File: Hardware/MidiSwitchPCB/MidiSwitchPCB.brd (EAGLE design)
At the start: 180 x 100 mm, 78 parts, among them IC3 74LVC2G04GW,125, J1 694108106102, J2 NMJ6HCD2, J3 NMJ6HCD2, J4 NMJ6HCD2, J5 NMJ6HCD2, Q1 BSS123, Q2 BSS123, Q3 BSS123, Q4 BSS123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

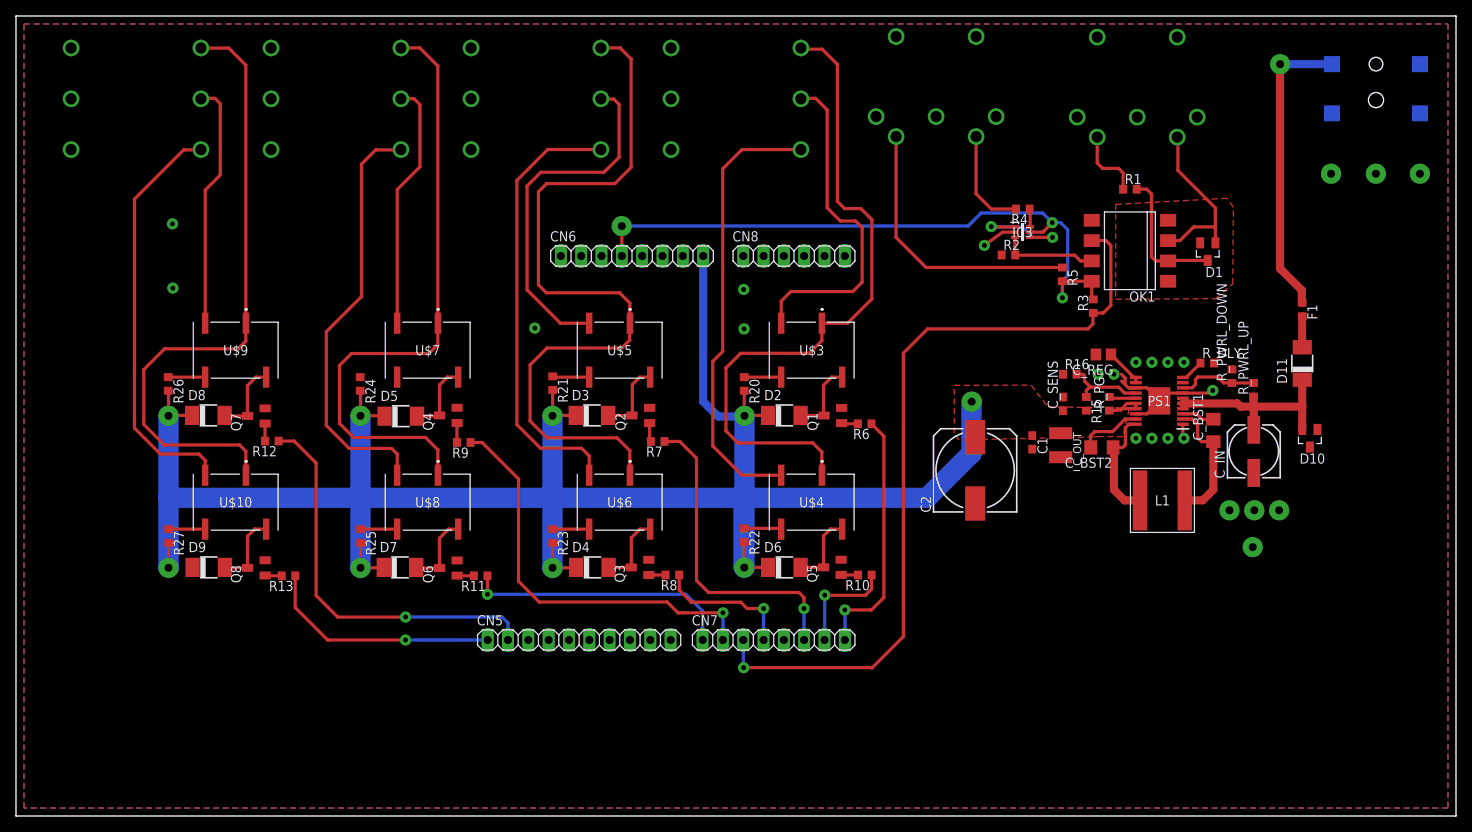
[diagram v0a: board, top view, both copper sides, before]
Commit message: Changed PCB size to 160 x 100
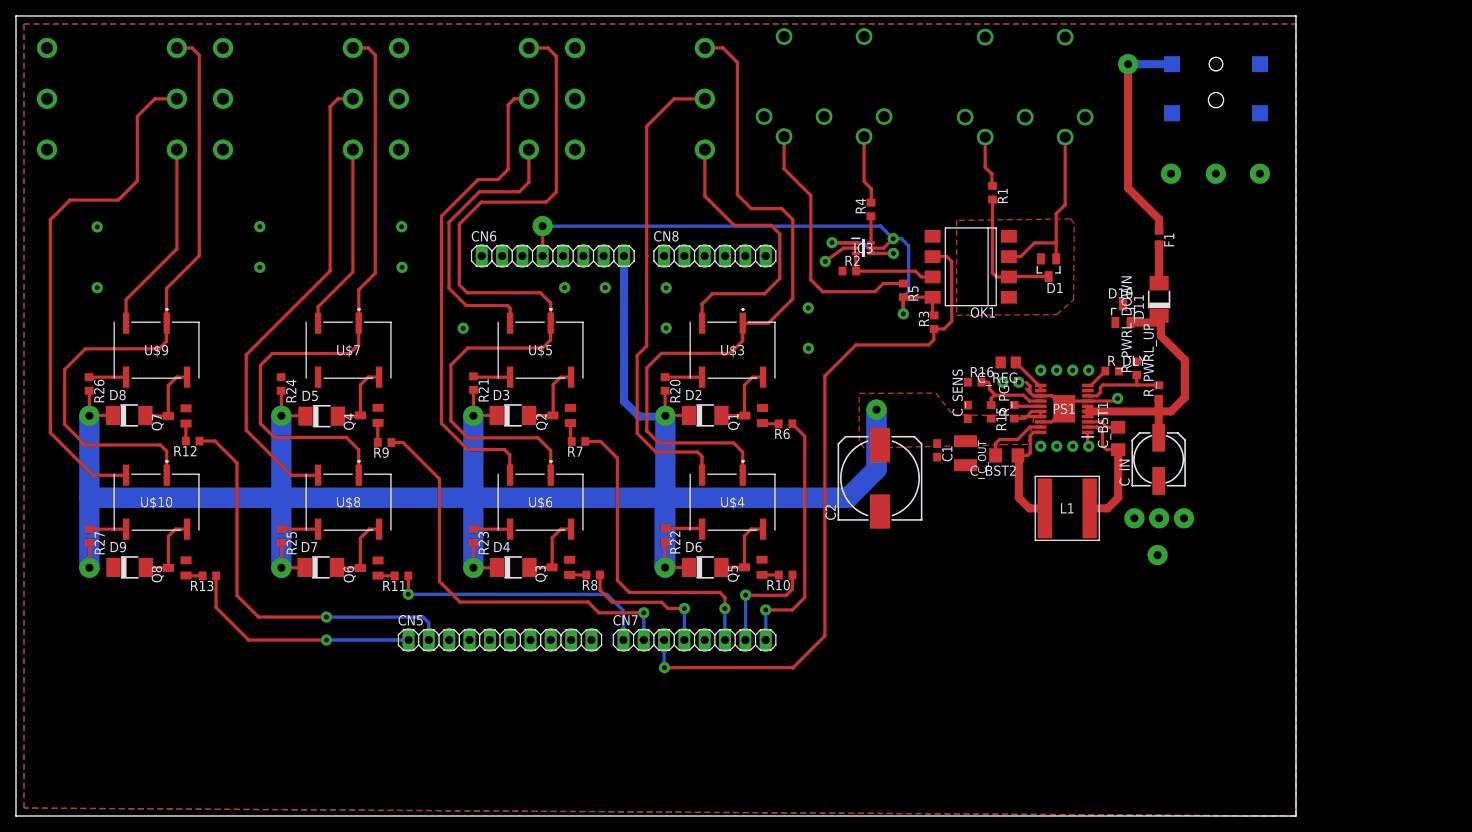
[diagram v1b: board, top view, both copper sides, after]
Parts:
- moved D10 28.1 mm to (138.4, 62.8), turned to 0 degrees
- moved F1 20.0 mm to (142.9, 72.3)
- moved J1 20.0 mm to (150.0, 90.9)
- moved D1 20.0 mm to (129.1, 68.5)
- moved IC3 20.0 mm to (105.9, 71.0)
- moved OK1 20.0 mm to (119.3, 68.7)
- moved R2 20.0 mm to (104.2, 68.1)
- moved R3 20.0 mm to (114.8, 61.7)
- moved R5 20.0 mm to (110.9, 65.7)
- moved D11 19.6 mm to (142.9, 64.6)
- moved R4 19.0 mm to (106.9, 75.8), turned to 90 degrees
- moved R1 17.2 mm to (122.1, 77.9), turned to 270 degrees
- moved U$1 14.0 mm to (126.2, 87.4)
- moved U$2 14.0 mm to (101.0, 87.4)
- moved J2 12.0 mm to (78.0, 100.0)
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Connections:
- removed net N$36: J2.5, U$3.4
- removed net N$37: J2.6, U$4.4
- removed net N$41: J5.5, U$9.4
- removed net N$50: J5.6, U$10.4
- new net N$2: J2.6, U$3.4
- new net N$28: J4.5, U$8.4
- new net N$4: J2.5, U$4.4
- new net N$6: J3.6, U$5.4
- net N$19: now also U$6.4; no longer U$5.4
- net N$22: now also J4.6, U$7.4; no longer J3.6, U$6.4
- net N$29: now also J5.6, U$9.4; no longer J4.6, U$8.4
- net N$30: now also J5.5, U$10.4; no longer J4.5, U$7.4
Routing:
- net N$28: track 0.00 -> 59.3 mm
- net N$4: track 0.00 -> 59.2 mm
- net N$37: track 56.0 -> 0.00 mm
- net N$50: track 51.9 -> 0.00 mm
- net N$36: track 42.2 -> 0.00 mm
- net N$2: track 0.00 -> 36.1 mm
- net N$6: track 0.00 -> 34.9 mm
- net N$30: track 31.2 -> 65.1 mm
- net N$22: track 55.7 -> 23.5 mm
- net N$41: track 30.9 -> 0.00 mm
- net N$29: track 53.2 -> 24.3 mm
- net N$19: track 44.6 -> 60.3 mm
- net N$9: track 99.8 -> 87.3 mm
- net VCC_3_3: track 81.2 -> 70.7 mm
- net VIN: track 37.5 -> 27.9 mm
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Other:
- board size 180 x 100 mm -> 160 x 100 mm
- board text removed: "Loch zu klein, passt nicht rein!"

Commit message: Created manufacturing documents
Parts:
- moved C_BST2 0.75 mm to (123.1, 44.9)
- moved C1 0.61 mm to (114.5, 45.6)
- moved C_OUT 0.43 mm to (118.3, 45.2)
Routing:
- net N$63: track 0.00 -> 4.62 mm
- net VCC_6-8: track 268.3 -> 271.9 mm, vias 10 -> 9
- net N$51: track 14.4 -> 15.3 mm
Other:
- board text added: "Midi Switch 2.0"

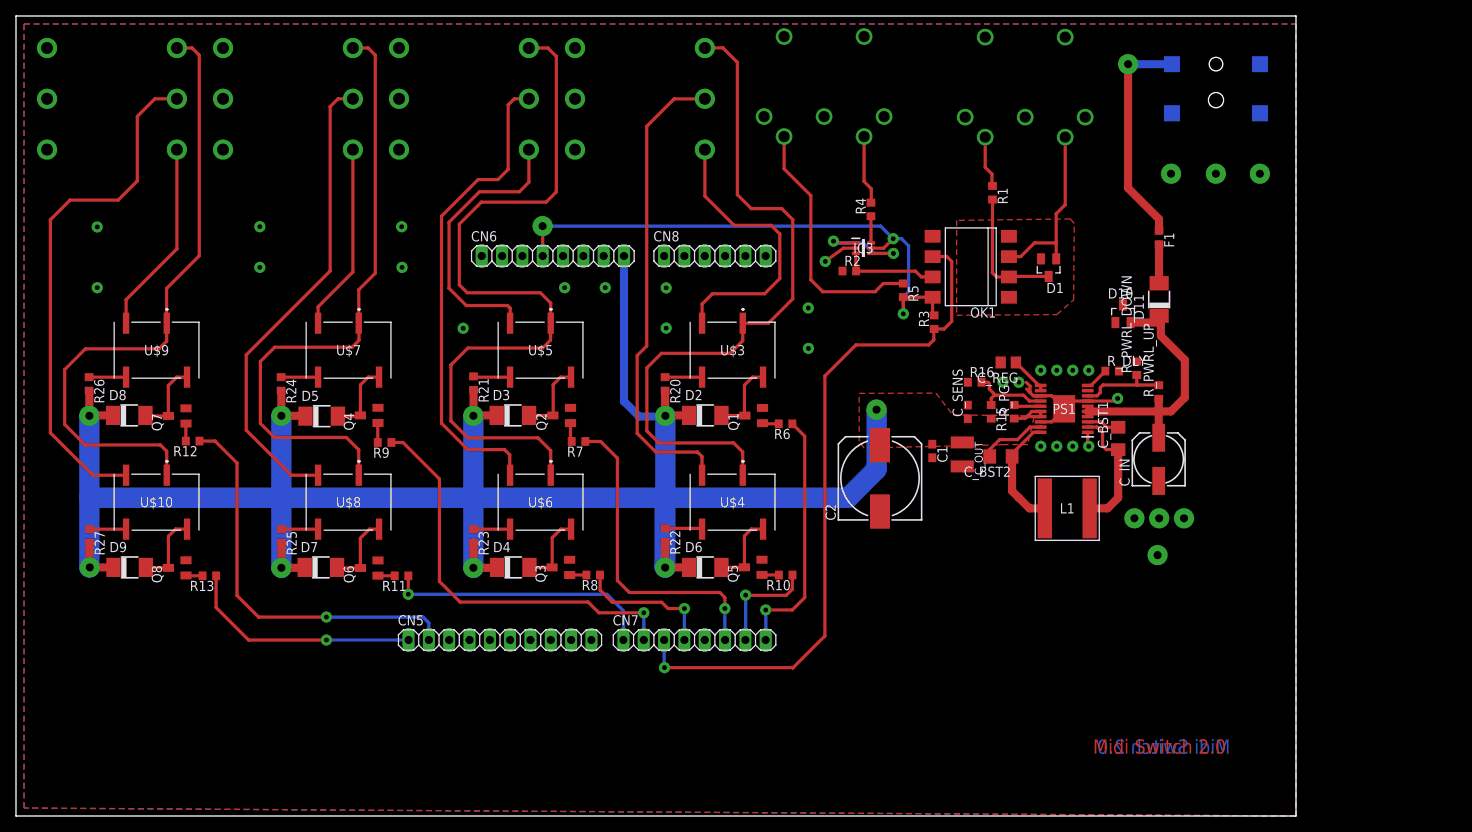
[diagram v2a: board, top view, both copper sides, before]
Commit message: Started reworking the layout before ordering it
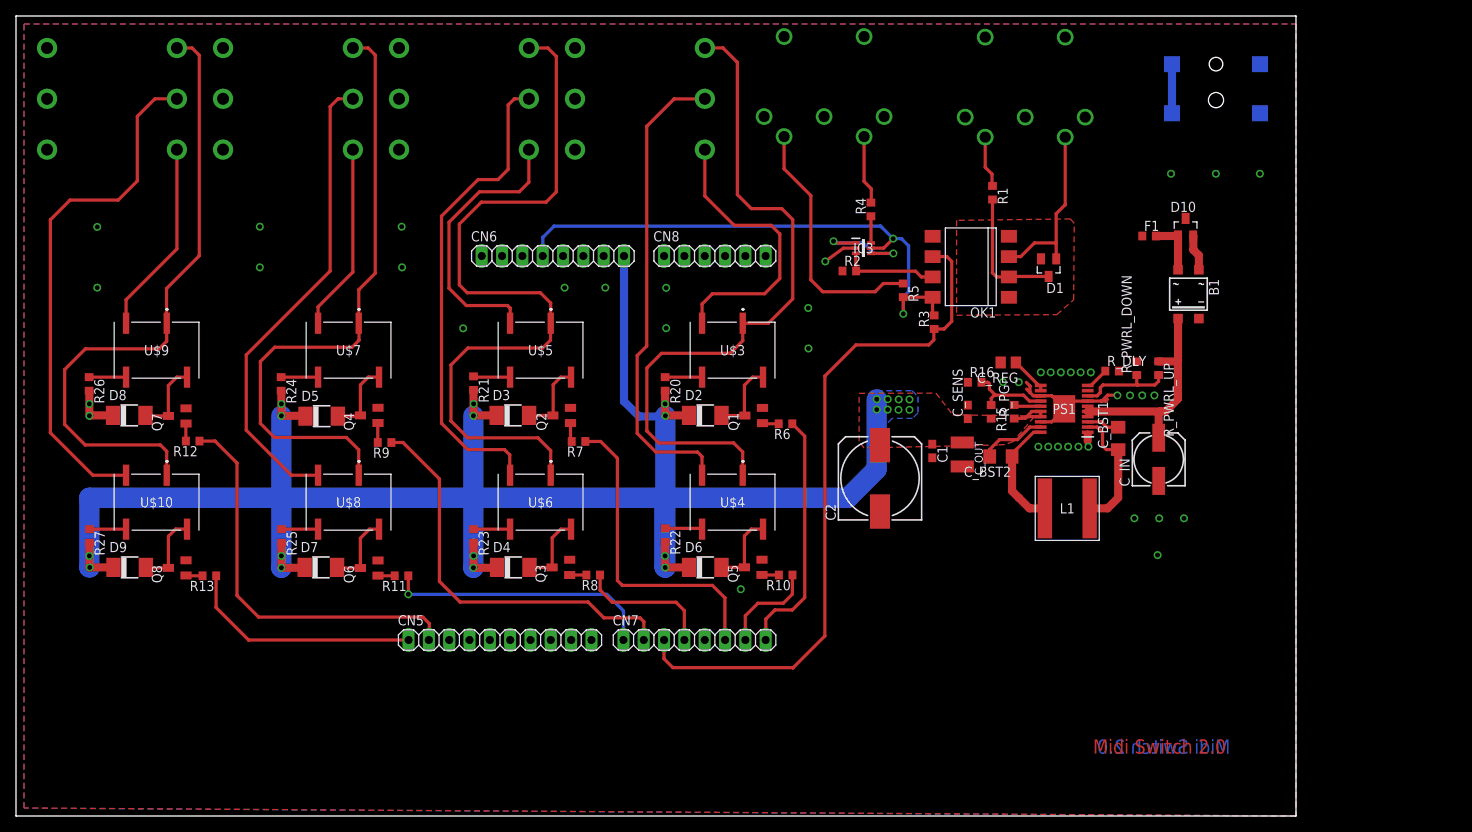
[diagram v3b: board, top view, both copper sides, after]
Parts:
- removed D11: (no value), diode:DO-214AC
- added B1: MB1S, rectifier:SOIC-4
- moved D10 13.4 mm to (146.2, 73.6)
- moved R_PWRL_UP 2.98 mm to (142.8, 56.0), turned to 270 degrees
- moved F1 1.26 mm to (141.6, 72.5), turned to 0 degrees
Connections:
- removed net N$66: D11.A, F1.2
- removed net VIN: F1.1, J1.1
- removed net VIN_FUSED: C_IN.+, D10.2, D11.C, PS1.4, PS1.5, PS1.6, R_PWRL_UP.1
- new net N$36: B1.~2, D10.1, F1.2
- new net N$37: B1.~1, D10.2, J1.3
- new net N$40: F1.1, J1.1, J1.2
- new net N$41: B1.+, C_IN.+, PS1.4, PS1.5, PS1.6, R_PWRL_UP.1
- net GND: now also B1.-; no longer D10.1, J1.3
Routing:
- net VIN_FUSED: track 34.6 -> 0.00 mm
- net N$41: track 0.00 -> 29.1 mm
- net VIN: track 27.9 -> 0.00 mm, vias 1 -> 0
- net VCC_6-8: track 271.9 -> 263.0 mm, vias 9 -> 20
- net N$36: track 0.00 -> 6.99 mm
- net N$40: track 0.00 -> 6.15 mm
- net N$66: track 4.87 -> 0.00 mm
- net N$37: track 0.00 -> 4.52 mm
- net CN7-7: track 13.6 -> 12.4 mm, vias 1 -> 0
- net N$58: track 11.1 -> 12.0 mm
- net VCC_3_3: track 70.7 -> 69.8 mm, vias 3 -> 2
- net CN7-8: track 31.6 -> 31.0 mm, vias 1 -> 0
- net CN7-2: track 51.3 -> 50.6 mm, vias 1 -> 0
- net N$9: track 87.3 -> 86.7 mm, vias 1 -> 0
- net GND: track 24.9 -> 25.2 mm, vias 32 -> 40
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- added copper zone on layer 16, net VCC_6-8

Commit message: finished layout reworking
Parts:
- IC3: value 74LVC2G04GW,125 -> 74LVC2G04GW
- PS1: value TPS55160QPWPTQ1 -> TPS55160
- U$10, U$3, U$4, U$5, U$6, U$7, U$8, U$9: value G6L-1F-TR_DC5-NEW -> Relay
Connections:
- net GND: now also CN5.7, CN6.6, CN6.7
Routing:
- net N$37: track 4.52 -> 30.7 mm, vias 0 -> 4
- net N$40: track 6.15 -> 27.4 mm, vias 0 -> 3
- net VCC_6-8: track 263.0 -> 269.6 mm, vias 20 -> 24
- net N$32: track 77.7 -> 75.4 mm
- net GND: track 25.2 -> 27.1 mm, vias 40 -> 63
- net N$38: track 86.4 -> 85.3 mm
- net N$30: track 65.1 -> 66.0 mm
- net N$28: track 59.3 -> 60.1 mm
- net CN7-6: track 39.8 -> 39.1 mm
- net N$9: track 86.7 -> 87.3 mm
- net VCC_6-1: track 0.04 -> 0.00 mm, vias 4 -> 0
- added copper zone on layer 1, net N$37
- added copper zone on layer 16, net N$37

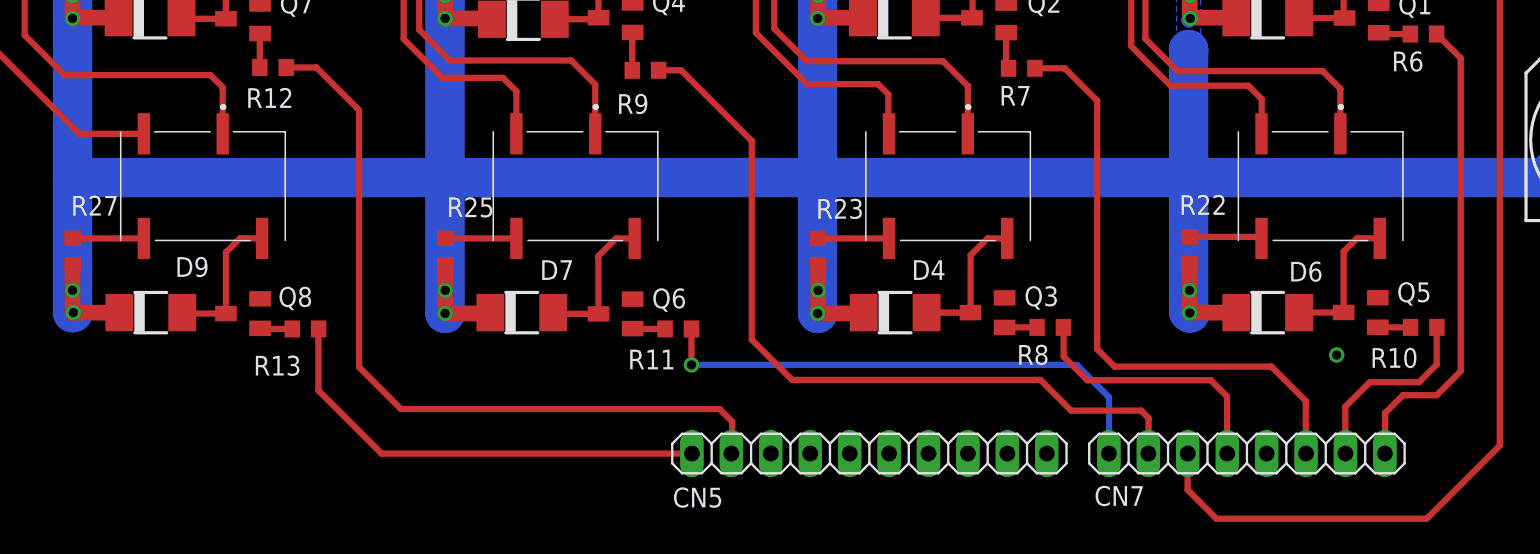
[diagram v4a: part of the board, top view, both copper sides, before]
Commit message: Debugged pin configuration causing device to be stuck in initialization. Debug code needs to be removed. Reverted pin config to previous pin config. Bug needs to be fixed in HW
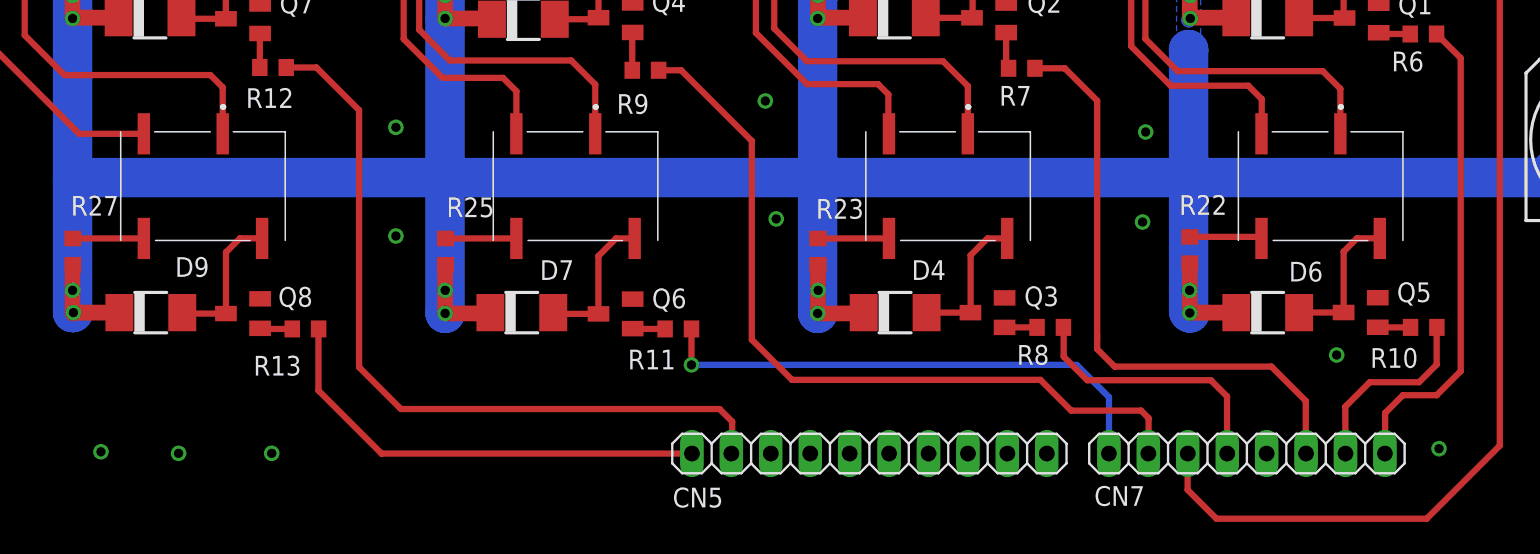
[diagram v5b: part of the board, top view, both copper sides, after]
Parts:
- renumbered U$1 to MIDI-IN, U$2 to MIDI-THRU
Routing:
- net GND: vias 63 -> 73
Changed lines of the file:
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@@
 <setting verticaltext="up"/>
 </settings>
-<grid distance="3.93700787" unitdist="mil" unit="mil" style="lines" multiple="1" display="yes" altdistance="3.93700787" altunitdist="mil" altunit="mil"/>
+<grid distance="0.1" unitdist="mm" unit="mm" style="lines" multiple="10" display="yes" altdistance="0.1" altunitdist="mil" altunit="mil"/>
 <layers>
 <layer number="1" name="Top" color="4" fill="1" visible="yes" active="yes"/>
@@
 <layer number="42" name="bRestrict" color="1" fill="10" visible="yes" active="yes"/>
 <layer number="43" name="vRestrict" color="2" fill="10" visible="yes" active="yes"/>
-<layer number="44" name="Drills" color="7" fill="1" visible="yes" active="yes"/>
+<layer number="44" name="Drills" color="7" fill="1" visible="no" active="yes"/>
 <layer number="45" name="Holes" color="7" fill="1" visible="yes" active="yes"/>
 <layer number="46" name="Milling" color="3" fill="1" visible="yes" active="yes"/>
@@
 </autorouter>
 <elements>
-<element name="U$2" library="MidiSwitchParts" package="MIDI_CONNECTOR_PAC" value="MIDI_CONNECTOR" x="101.01" y="87.43" smashed="yes" rot="MR0"/>
-<element name="U$1" library="MidiSwitchParts" package="MIDI_CONNECTOR_PAC" value="MIDI_CONNECTOR" x="126.15" y="87.36" smashed="yes" rot="MR0"/>
+<element name="MIDI-THRU" library="MidiSwitchParts" package="MIDI_CONNECTOR_PAC" value="MIDI_CONNECTOR" x="101.01" y="87.43" smashed="yes" rot="MR0"/>
+<element name="MIDI-IN" library="MidiSwitchParts" package="MIDI_CONNECTOR_PAC" value="MIDI_CONNECTOR" x="126.15" y="87.36" smashed="yes" rot="MR0"/>
 <element name="OK1" library="6N138S" package="DIL8-SMD" value="6N138S" x="119.3488" y="68.6516" smashed="yes" rot="R90">
 <attribute name="VALUE" x="122.5238" y="75.0016" size="1.27" layer="27" ratio="10" rot="R180"/>
@@
 <signals>
 <signal name="N$3" class="3">
-<contactref element="U$1" pad="P4"/>
+<contactref element="MIDI-IN" pad="P4"/>
 <contactref element="R1" pad="1"/>
 <wire x1="122.0622" y1="78.7612" x2="121.9962" y2="78.8272" width="0.4064" layer="1"/>
@@
 </signal>
 <signal name="N$8" class="3">
-<contactref element="U$1" pad="P5"/>
+<contactref element="MIDI-IN" pad="P5"/>
 <contactref element="OK1" pad="3"/>
 <contactref element="D1" pad="1"/>
@@
 <contactref element="R2" pad="1"/>
 <contactref element="OK1" pad="5"/>
-<contactref element="U$1" pad="P7"/>
-<contactref element="U$1" pad="P6"/>
+<contactref element="MIDI-IN" pad="P7"/>
+<contactref element="MIDI-IN" pad="P6"/>
 <contactref element="Q1" pad="2"/>
 <contactref element="Q5" pad="2"/>
@@
 <via x="40.46" y="63.48" extent="1-16" drill="0.6"/>
 <via x="16.48" y="64.48" extent="1-16" drill="0.6"/>
+<via x="21.9974" y="22.013" extent="1-16" drill="0.6"/>
+<via x="10.9974" y="22.113" extent="1-16" drill="0.6"/>
+<via x="15.9974" y="22.013" extent="1-16" drill="0.6"/>
+<via x="29.9974" y="36.013" extent="1-16" drill="0.6"/>
+<via x="29.9974" y="43.013" extent="1-16" drill="0.6"/>
+<via x="53.7974" y="44.713" extent="1-16" drill="0.6"/>
+<via x="54.4974" y="37.113" extent="1-16" drill="0.6"/>
+<via x="78.0974" y="36.913" extent="1-16" drill="0.6"/>
+<via x="78.2974" y="42.713" extent="1-16" drill="0.6"/>
+<via x="97.1974" y="22.313" extent="1-16" drill="0.6"/>
 </signal>
 <signal name="N$5">
-<contactref element="U$2" pad="P4"/>
+<contactref element="MIDI-THRU" pad="P4"/>
 <contactref element="R5" pad="1"/>
 <wire x1="110.9056" y1="66.562" x2="108.4118" y2="66.562" width="0.4064" layer="1"/>
@@
 <signal name="N$10">
 <contactref element="R4" pad="2"/>
-<contactref element="U$2" pad="P5"/>
+<contactref element="MIDI-THRU" pad="P5"/>
 <wire x1="106.8666" y1="76.6722" x2="106.9086" y2="76.7142" width="0.4064" layer="1"/>
 <wire x1="106.9086" y1="76.7142" x2="106.9086" y2="78.4098" width="0.4064" layer="1"/>
